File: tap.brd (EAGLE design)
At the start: 20.3 x 57.5 mm, 4 parts

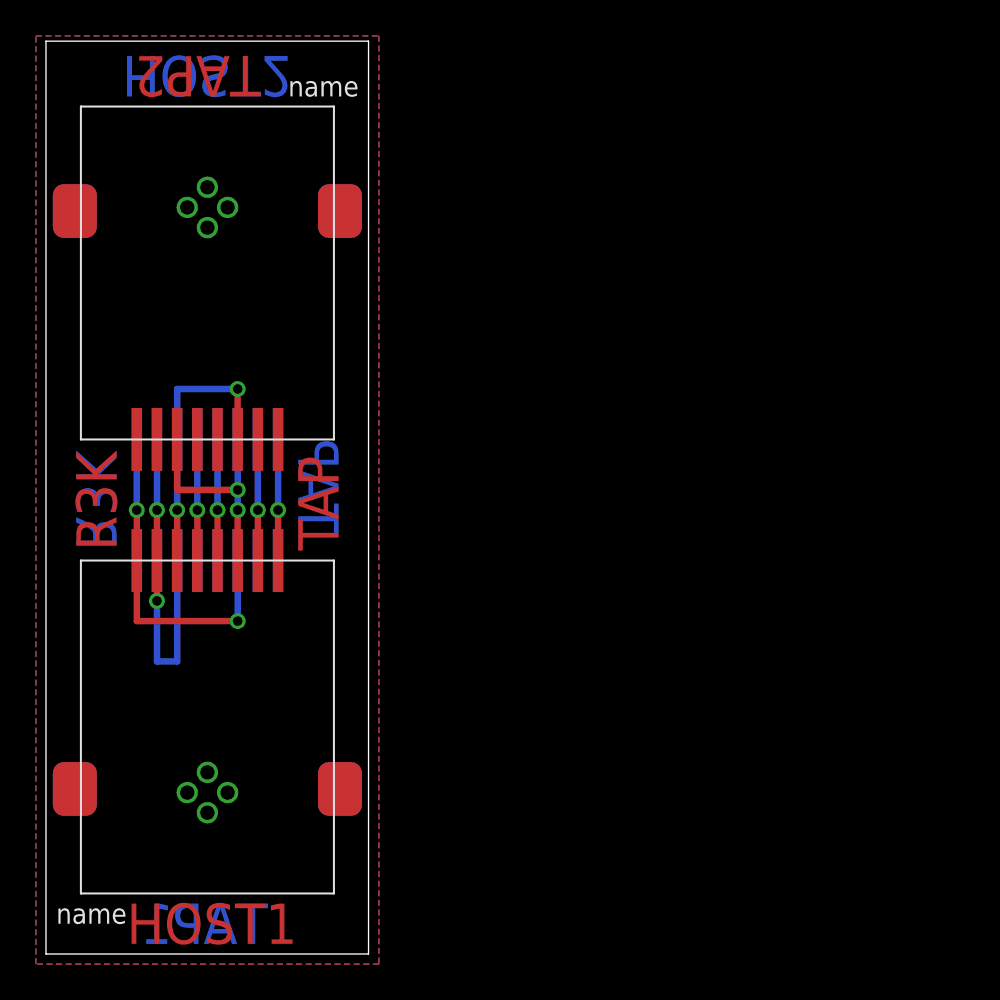
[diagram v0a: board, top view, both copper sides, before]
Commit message: Fixing some minor pseudobug and rotating the whole board
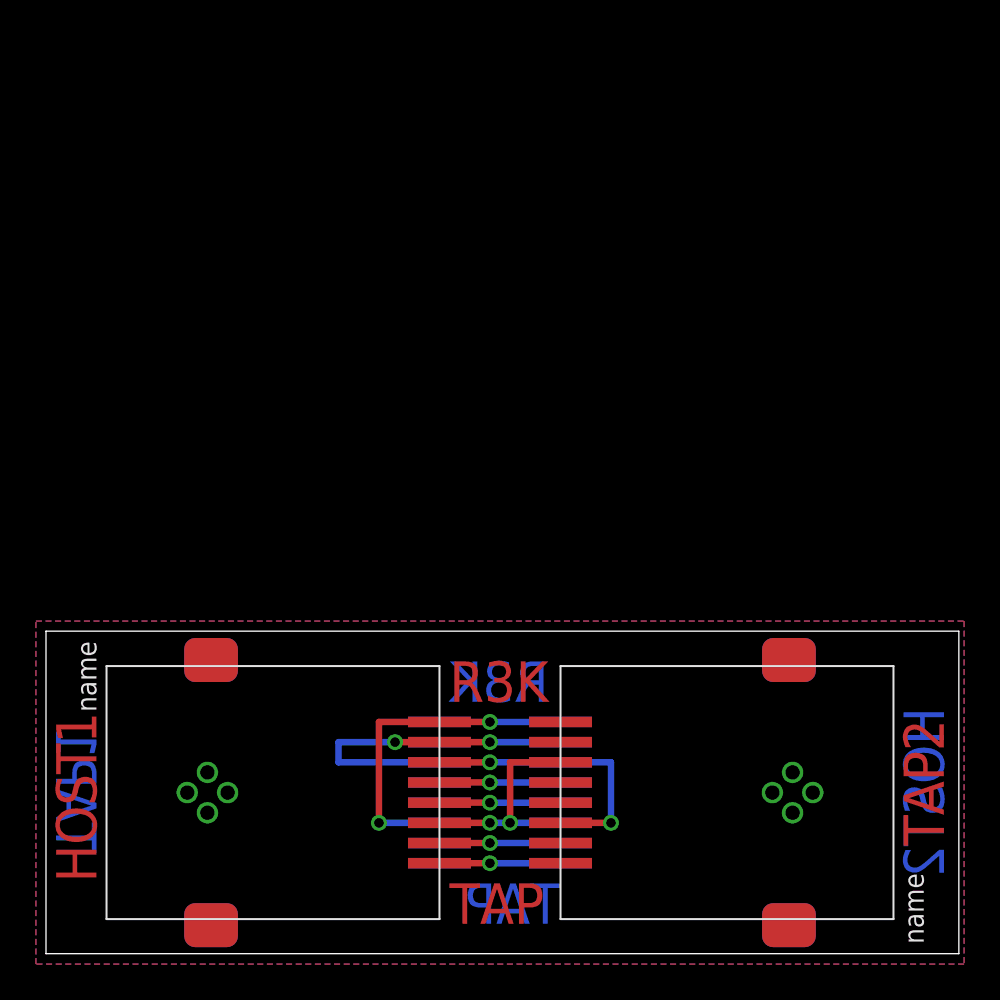
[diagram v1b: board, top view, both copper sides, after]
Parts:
- moved HOST2 37.7 mm to (36.8, 10.2), turned to 270 degrees
- moved TAP2 37.7 mm to (36.8, 10.2), turned to 90 degrees
- moved HOST1 14.4 mm to (20.3, 10.2), turned to 270 degrees
- moved TAP1 14.4 mm to (20.3, 10.2), turned to 90 degrees
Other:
- board size 20.3 x 57.5 mm -> 57.5 x 20.3 mm
